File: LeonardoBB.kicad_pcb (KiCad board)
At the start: 2 copper layers, 48 x 58 mm, 43 parts, among them J1 USB_B_Micro, J2 Conn_01x17, J3 Conn_01x17, J4 I2C, Q1 Q_PMOS_GSD, Q2 Q_DUAL_PMOS_S1G1D2S2G2D1, SW1 SW_SPDT, U1 ATmega32U4-MU, U2 LMV358, U3 NCP1117-5.0_SOT223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

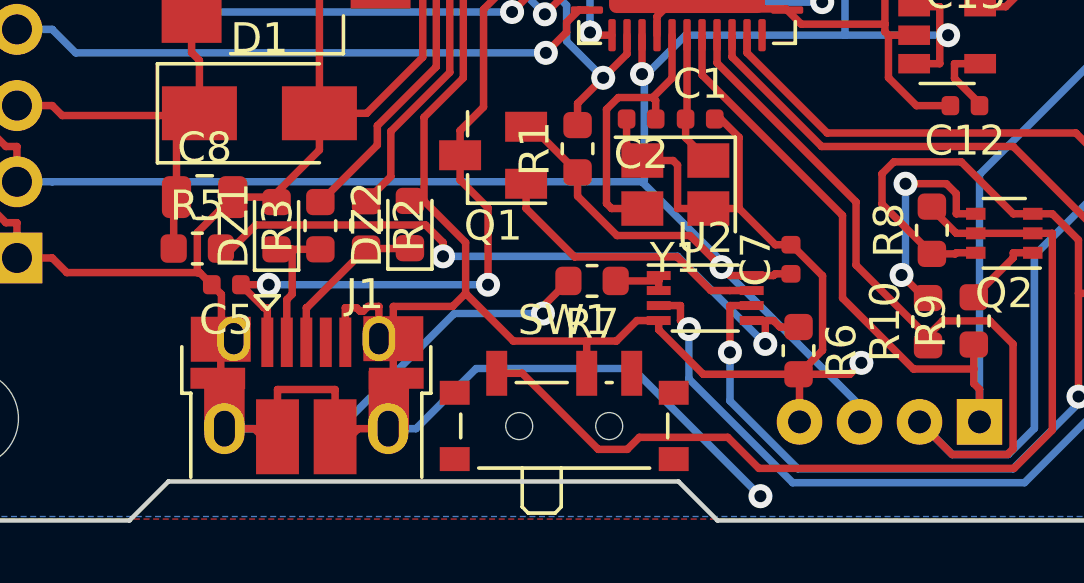
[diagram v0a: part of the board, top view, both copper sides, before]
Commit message: Change footprints for USB and LMV358
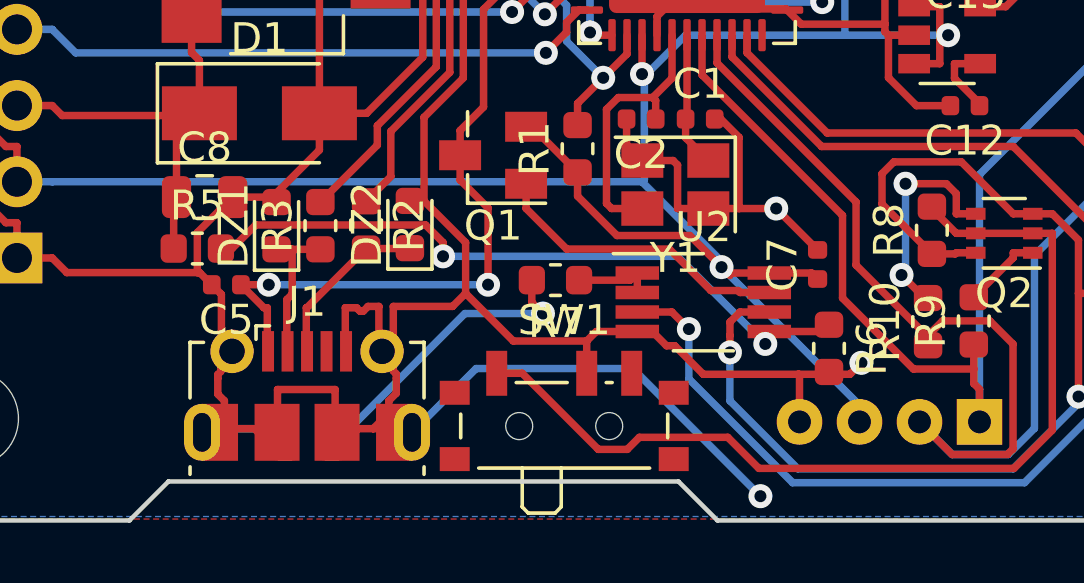
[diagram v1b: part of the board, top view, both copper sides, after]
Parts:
- J1: footprint Connector_USB:USB_Micro-B_Amphenol_10103594-0001LF_Horizontal -> Connector_USB:USB_Micro-B_Molex-105017-0001
- U2: footprint Package_SO:VSSOP-8_2.3x2mm_P0.5mm -> Package_SO:VSSOP-8_3.0x3.0mm_P0.65mm
- moved R7 1.22 mm to (142.9, 120.0)
- moved R6 1.02 mm to (152.0, 122.3)
- moved C7 0.91 mm to (151.6, 119.5)
- moved U2 0.15 mm to (147.8, 120.7)
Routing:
- net GND: track 301.4 -> 296.8 mm, vias 7 -> 8
- net +5V: track 134.2 -> 135.5 mm
- net Net-(R7-Pad1): track 1.93 -> 2.69 mm
- net Net-(Q1-Pad1): track 9.48 -> 10.1 mm

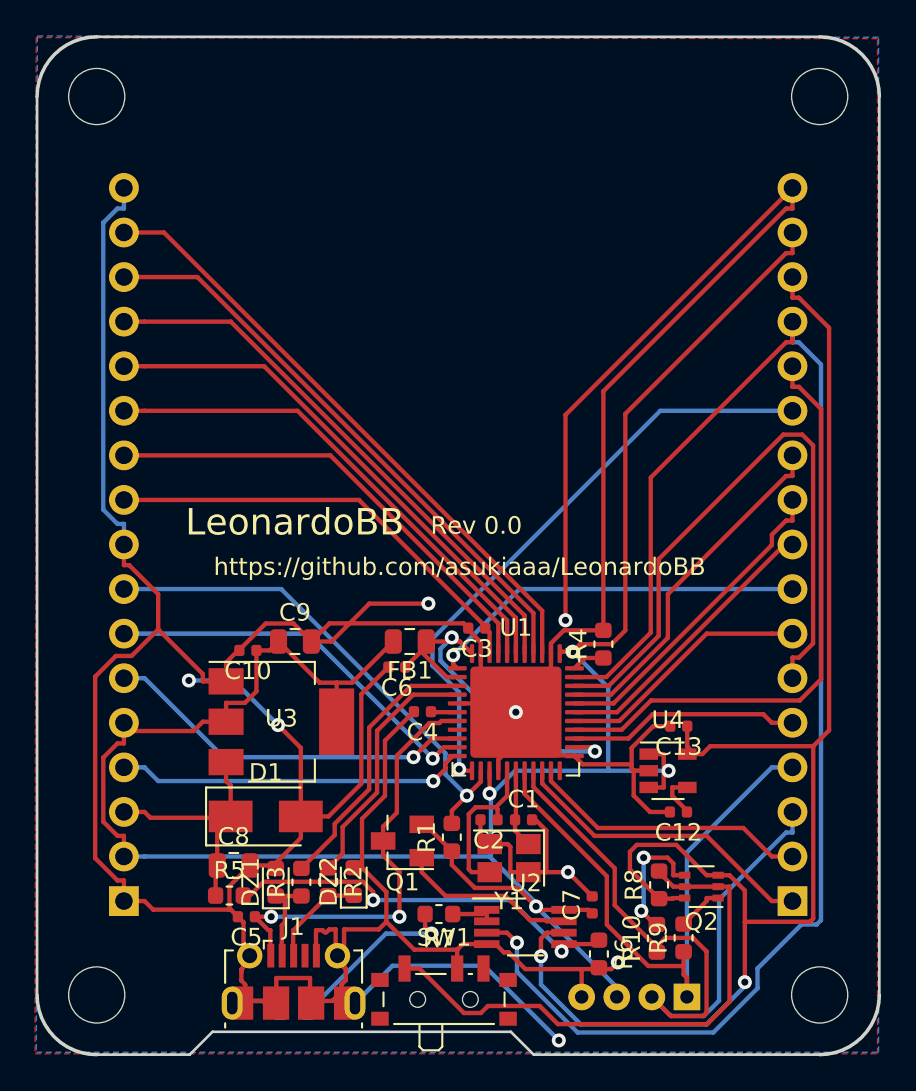
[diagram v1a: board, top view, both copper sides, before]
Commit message: Update silks as revision 2019.03
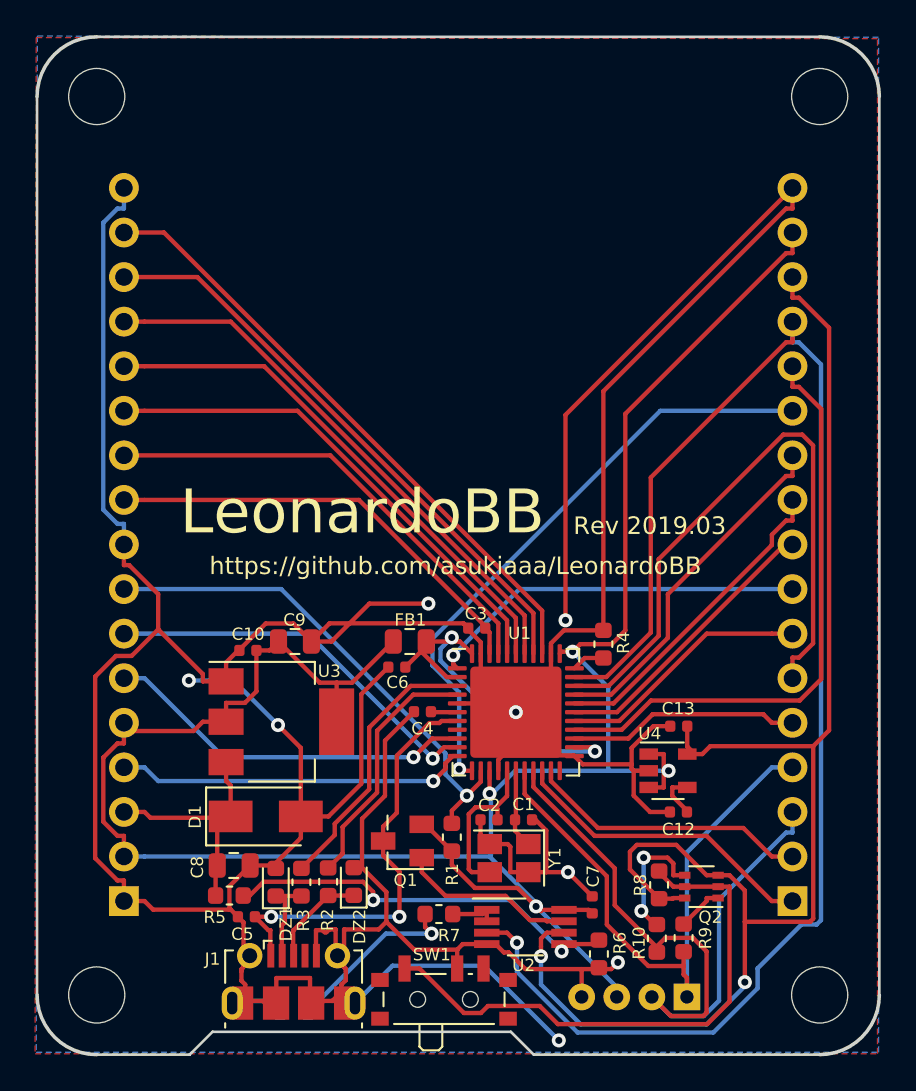
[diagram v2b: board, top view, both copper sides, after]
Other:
- board text added: "*"
- board text added: "0"
- board text added: "1"
- board text added: "10"
- board text added: "11"
- board text added: "12"
- board text added: "13"
- board text added: "2"
- board text added: "3"
- board text added: "4"
- board text added: "5"
- board text added: "6"
- board text added: "7"
- board text added: "8"
- board text added: "9"
- board text added: "Rev 2019.03"
- board text added: "Rev2019.03"
- board text removed: "D0"
- board text removed: "D1"
- board text removed: "D10"
- board text removed: "D11"
- board text removed: "D12"
- board text removed: "D13"
- board text removed: "D2"
- board text removed: "D3"
- board text removed: "D4"
- board text removed: "D5"
- board text removed: "D6"
- board text removed: "D7"
- board text removed: "D8"
- board text removed: "D9"
- board text removed: "PWM"
- board text removed: "Rev 0.0"
- board text removed: "Rev0.0"
